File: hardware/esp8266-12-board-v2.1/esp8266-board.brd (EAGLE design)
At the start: 32.9 x 31.4 mm, 29 parts, among them J1 DEBUG, J2 WATCHDOG, P3 GND DTR RTS RX TX

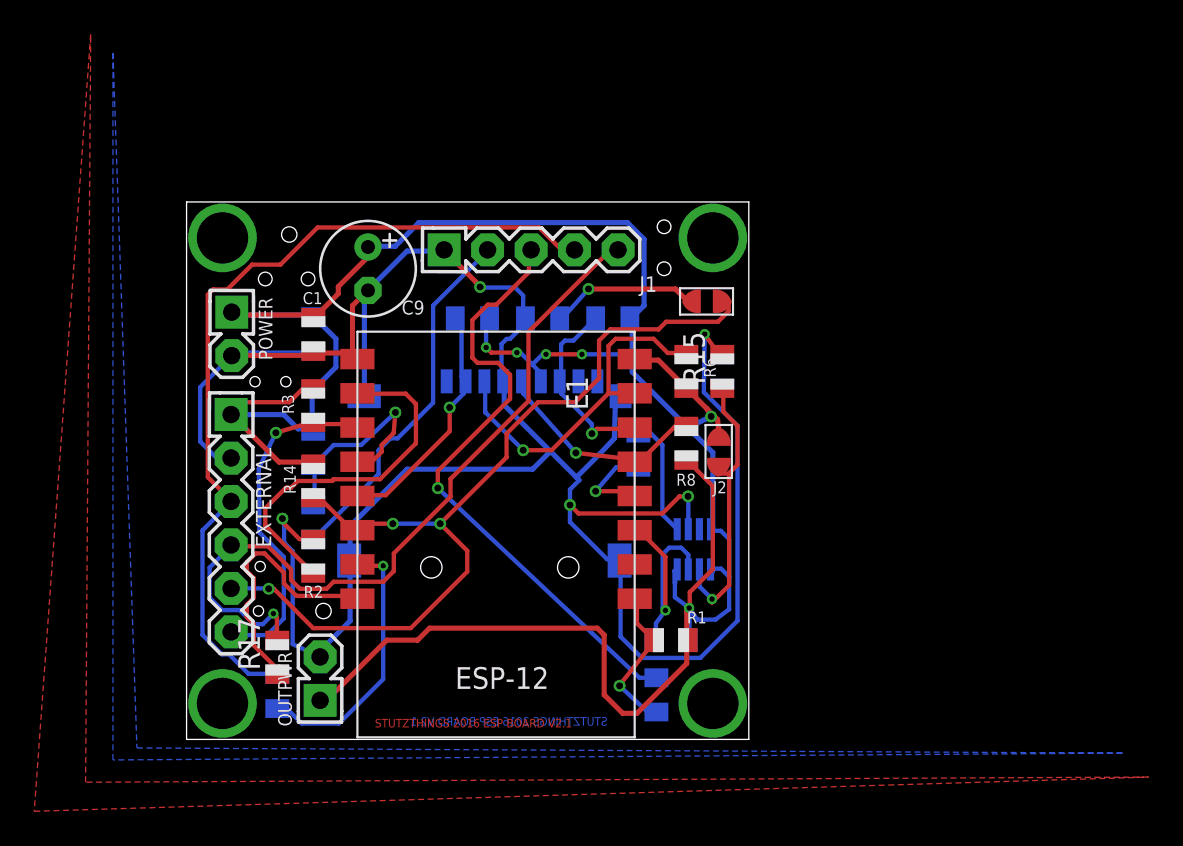
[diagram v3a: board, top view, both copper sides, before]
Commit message: esp8266 2.1 pcb sent to seeed studio
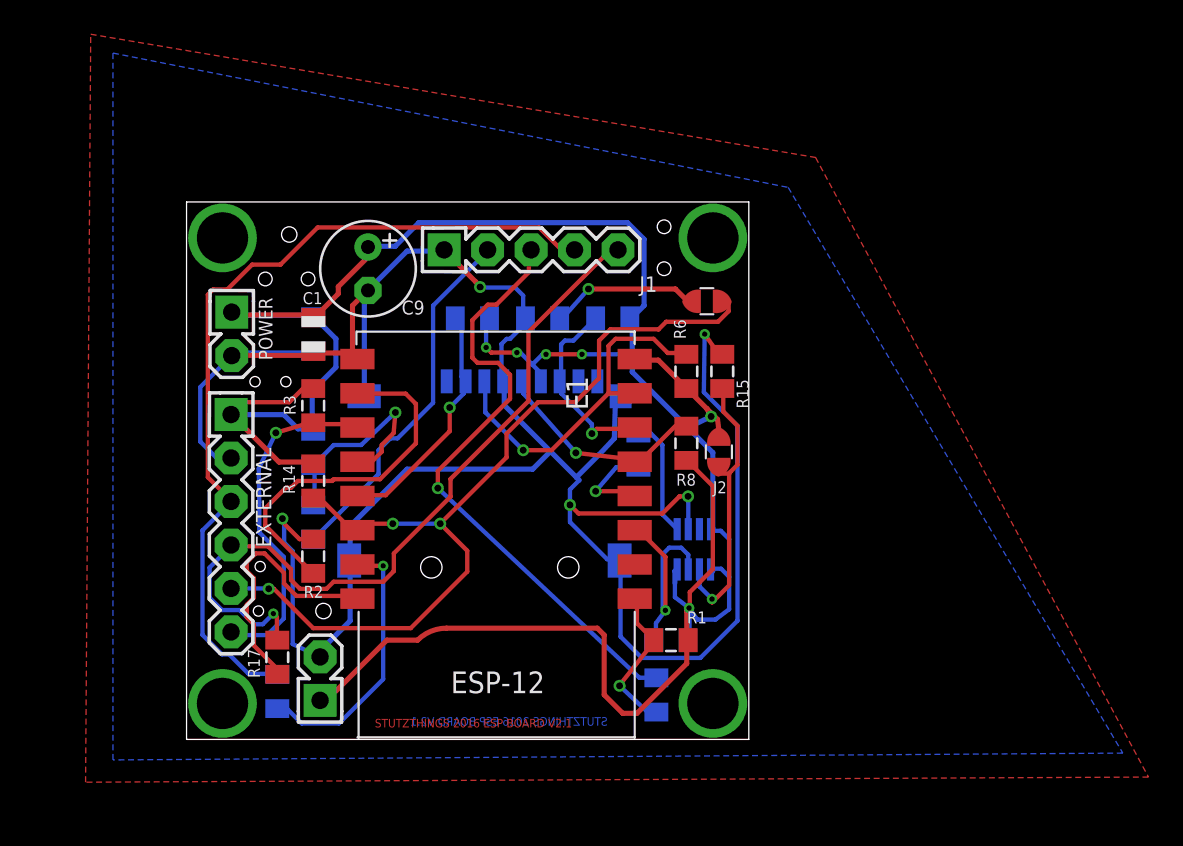
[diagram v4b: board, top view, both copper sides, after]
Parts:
- C1, C3: device stutz-components-library:SMD0805 -> stutz-components-library:SMD0805@1

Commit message: updated pcb after first manufacturing impressions
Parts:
- C1: value 0.1uF -> 100nF; device stutz-components-library:SMD0805@1 -> stutz-components-library:SMD0805
- C3: device stutz-components-library:SMD0805@1 -> stutz-components-library:SMD0805
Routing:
- net N$6: track 9.26 -> 10.3 mm
- net ESP_GPIO5: track 52.7 -> 53.3 mm
- net +3.3V: track 155.0 -> 155.6 mm
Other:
- board text added: "+3.3V"
- board text added: "DTR"
- board text added: "GND"
- board text added: "IO2"
- board text added: "IO5"
- board text added: "RTS"
- board text added: "RX"
- board text added: "TX"
